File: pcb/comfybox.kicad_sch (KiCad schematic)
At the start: 20 parts, among them K1 SW_CHOC, K2 SW_CHOC, K3 SW_CHOC, K4 SW_CHOC, P1 SW_CHOC, P2 SW_CHOC, P3 SW_CHOC, P4 SW_CHOC

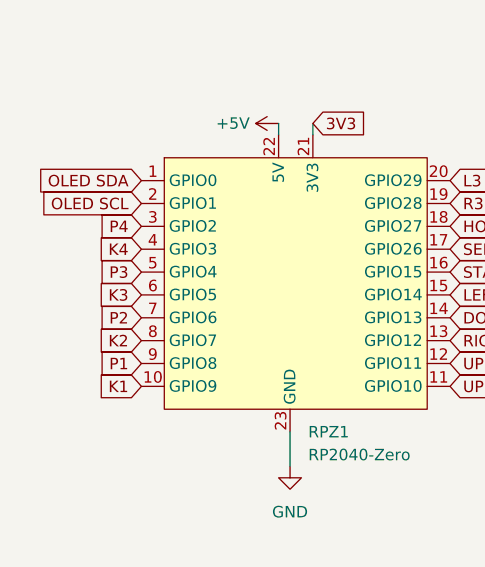
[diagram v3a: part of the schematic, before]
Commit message: improve spacing and redo tracing
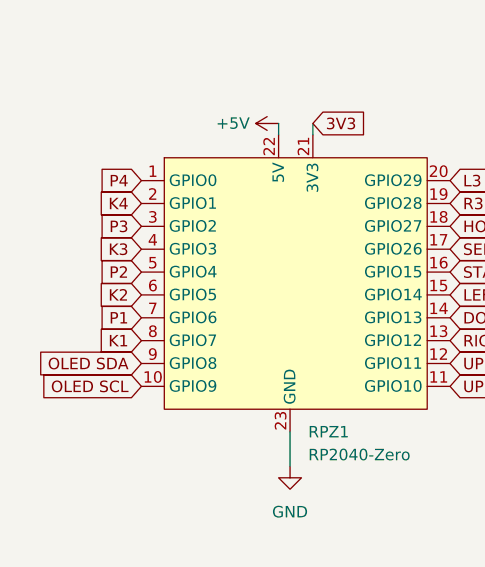
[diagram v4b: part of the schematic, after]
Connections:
- net K1: now also RPZ1.8 (GPIO7); no longer RPZ1.10 (GPIO9)
- net K2: now also RPZ1.6 (GPIO5); no longer RPZ1.8 (GPIO7)
- net K3: now also RPZ1.4 (GPIO3); no longer RPZ1.6 (GPIO5)
- net K4: now also RPZ1.2 (GPIO1); no longer RPZ1.4 (GPIO3)
- net OLED SCL: now also RPZ1.10 (GPIO9); no longer RPZ1.2 (GPIO1)
- net OLED SDA: now also RPZ1.9 (GPIO8); no longer RPZ1.1 (GPIO0)
- net P1: now also RPZ1.7 (GPIO6); no longer RPZ1.9 (GPIO8)
- net P2: now also RPZ1.5 (GPIO4); no longer RPZ1.7 (GPIO6)
- net P3: now also RPZ1.3 (GPIO2); no longer RPZ1.5 (GPIO4)
- net P4: now also RPZ1.1 (GPIO0); no longer RPZ1.3 (GPIO2)
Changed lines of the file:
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@@
     )
   )
-  (global_label "K4" (shape input) (at 45.72 64.77 180) (fields_autoplaced)
+  (global_label "K4" (shape input) (at 45.72 59.69 180) (fields_autoplaced)
     (effects (font (size 1.27 1.27)) (justify right))
-    (property "Intersheet References" "${INTERSHEET_REFS}" (id 0) (at 40.8274 64.6906 0)
+    (property "Intersheet References" "${INTERSHEET_REFS}" (id 0) (at 40.8274 59.6106 0)
       (effects (font (size 1.27 1.27)) (justify right) hide)
     )
@@
     )
   )
-  (global_label "OLED SDA" (shape input) (at 45.72 57.15 180) (fields_autoplaced)
+  (global_label "OLED SDA" (shape input) (at 45.72 77.47 180) (fields_autoplaced)
     (effects (font (size 1.27 1.27)) (justify right))
-    (property "Intersheet References" "${INTERSHEET_REFS}" (id 0) (at 33.9936 57.0706 0)
+    (property "Intersheet References" "${INTERSHEET_REFS}" (id 0) (at 33.9936 77.3906 0)
       (effects (font (size 1.27 1.27)) (justify right) hide)
     )
@@
     )
   )
-  (global_label "P4" (shape input) (at 45.72 62.23 180) (fields_autoplaced)
+  (global_label "P4" (shape input) (at 45.72 57.15 180) (fields_autoplaced)
     (effects (font (size 1.27 1.27)) (justify right))
-    (property "Intersheet References" "${INTERSHEET_REFS}" (id 0) (at 40.8274 62.1506 0)
+    (property "Intersheet References" "${INTERSHEET_REFS}" (id 0) (at 40.8274 57.0706 0)
       (effects (font (size 1.27 1.27)) (justify right) hide)
     )
@@
     )
   )
-  (global_label "P1" (shape input) (at 45.72 77.47 180) (fields_autoplaced)
+  (global_label "P1" (shape input) (at 45.72 72.39 180) (fields_autoplaced)
     (effects (font (size 1.27 1.27)) (justify right))
-    (property "Intersheet References" "${INTERSHEET_REFS}" (id 0) (at 40.8274 77.3906 0)
+    (property "Intersheet References" "${INTERSHEET_REFS}" (id 0) (at 40.8274 72.3106 0)
       (effects (font (size 1.27 1.27)) (justify right) hide)
     )
@@
     )
   )
-  (global_label "K3" (shape input) (at 45.72 69.85 180) (fields_autoplaced)
+  (global_label "K3" (shape input) (at 45.72 64.77 180) (fields_autoplaced)
     (effects (font (size 1.27 1.27)) (justify right))
-    (property "Intersheet References" "${INTERSHEET_REFS}" (id 0) (at 40.8274 69.7706 0)
+    (property "Intersheet References" "${INTERSHEET_REFS}" (id 0) (at 40.8274 64.6906 0)
       (effects (font (size 1.27 1.27)) (justify right) hide)
     )
   )
-  (global_label "P2" (shape input) (at 45.72 72.39 180) (fields_autoplaced)
+  (global_label "P2" (shape input) (at 45.72 67.31 180) (fields_autoplaced)
     (effects (font (size 1.27 1.27)) (justify right))
-    (property "Intersheet References" "${INTERSHEET_REFS}" (id 0) (at 40.8274 72.3106 0)
+    (property "Intersheet References" "${INTERSHEET_REFS}" (id 0) (at 40.8274 67.2306 0)
       (effects (font (size 1.27 1.27)) (justify right) hide)
     )
@@
     )
   )
-  (global_label "K1" (shape input) (at 45.72 80.01 180) (fields_autoplaced)
+  (global_label "K1" (shape input) (at 45.72 74.93 180) (fields_autoplaced)
     (effects (font (size 1.27 1.27)) (justify right))
-    (property "Intersheet References" "${INTERSHEET_REFS}" (id 0) (at 40.8274 79.9306 0)
+    (property "Intersheet References" "${INTERSHEET_REFS}" (id 0) (at 40.8274 74.8506 0)
       (effects (font (size 1.27 1.27)) (justify right) hide)
     )
   )
-  (global_label "P3" (shape input) (at 45.72 67.31 180) (fields_autoplaced)
+  (global_label "P3" (shape input) (at 45.72 62.23 180) (fields_autoplaced)
     (effects (font (size 1.27 1.27)) (justify right))
-    (property "Intersheet References" "${INTERSHEET_REFS}" (id 0) (at 40.8274 67.2306 0)
+    (property "Intersheet References" "${INTERSHEET_REFS}" (id 0) (at 40.8274 62.1506 0)
       (effects (font (size 1.27 1.27)) (justify right) hide)
     )
@@
     )
   )
-  (global_label "K2" (shape input) (at 45.72 74.93 180) (fields_autoplaced)
+  (global_label "K2" (shape input) (at 45.72 69.85 180) (fields_autoplaced)
     (effects (font (size 1.27 1.27)) (justify right))
-    (property "Intersheet References" "${INTERSHEET_REFS}" (id 0) (at 40.8274 74.8506 0)
+    (property "Intersheet References" "${INTERSHEET_REFS}" (id 0) (at 40.8274 69.7706 0)
       (effects (font (size 1.27 1.27)) (justify right) hide)
     )
@@
     )
   )
-  (global_label "OLED SCL" (shape input) (at 45.72 59.69 180) (fields_autoplaced)
+  (global_label "OLED SCL" (shape input) (at 45.72 80.01 180) (fields_autoplaced)
     (effects (font (size 1.27 1.27)) (justify right))
-    (property "Intersheet References" "${INTERSHEET_REFS}" (id 0) (at 34.054 59.6106 0)
+    (property "Intersheet References" "${INTERSHEET_REFS}" (id 0) (at 34.054 79.9306 0)
       (effects (font (size 1.27 1.27)) (justify right) hide)
     )

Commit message: update libs and add KS33 support
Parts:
- DOWN1, K1, K2, K3, K4, LEFT1, P1, P2, P3, P4, RIGHT1, UP1, UP2: footprint Kailh:Kailh_socket_PG1350_optional -> Switch:Kailh_PG1350_Gateron_KS27_KS33
- OLED1: footprint SSD1306:128x64OLED -> OLED:SSD1306-128x64_OLED
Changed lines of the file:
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@@
     (property "Reference" "LEFT1" (id 0) (at 120.65 64.77 0))
     (property "Value" "SW_CHOC" (id 1) (at 120.65 67.31 0))
-    (property "Footprint" "Kailh:Kailh_socket_PG1350_optional" (id 2) (at 120.65 67.31 0)
+    (property "Footprint" "Switch:Kailh_PG1350_Gateron_KS27_KS33" (id 2) (at 120.65 67.31 0)
       (effects (font (size 1.27 1.27)) hide)
     )
@@
     (property "Reference" "K4" (id 0) (at 181.61 111.76 0))
     (property "Value" "SW_CHOC" (id 1) (at 181.61 114.3 0))
-    (property "Footprint" "Kailh:Kailh_socket_PG1350_optional" (id 2) (at 181.61 114.3 0)
+    (property "Footprint" "Switch:Kailh_PG1350_Gateron_KS27_KS33" (id 2) (at 181.61 114.3 0)
       (effects (font (size 1.27 1.27)) hide)
     )
@@
     (property "Reference" "K2" (id 0) (at 140.97 111.76 0))
     (property "Value" "SW_CHOC" (id 1) (at 140.97 114.3 0))
-    (property "Footprint" "Kailh:Kailh_socket_PG1350_optional" (id 2) (at 140.97 114.3 0)
+    (property "Footprint" "Switch:Kailh_PG1350_Gateron_KS27_KS33" (id 2) (at 140.97 114.3 0)
       (effects (font (size 1.27 1.27)) hide)
     )
@@
     (property "Reference" "UP2" (id 0) (at 201.93 64.77 0))
     (property "Value" "SW_CHOC" (id 1) (at 201.93 67.31 0))
-    (property "Footprint" "Kailh:Kailh_socket_PG1350_optional" (id 2) (at 201.93 67.31 0)
+    (property "Footprint" "Switch:Kailh_PG1350_Gateron_KS27_KS33" (id 2) (at 201.93 67.31 0)
       (effects (font (size 1.27 1.27)) hide)
     )
@@
     (property "Reference" "P1" (id 0) (at 120.65 90.17 0))
     (property "Value" "SW_CHOC" (id 1) (at 120.65 92.71 0))
-    (property "Footprint" "Kailh:Kailh_socket_PG1350_optional" (id 2) (at 120.65 92.71 0)
+    (property "Footprint" "Switch:Kailh_PG1350_Gateron_KS27_KS33" (id 2) (at 120.65 92.71 0)
       (effects (font (size 1.27 1.27)) hide)
     )
@@
     (property "Reference" "K3" (id 0) (at 161.29 111.76 0))
     (property "Value" "SW_CHOC" (id 1) (at 161.29 114.3 0))
-    (property "Footprint" "Kailh:Kailh_socket_PG1350_optional" (id 2) (at 161.29 114.3 0)
+    (property "Footprint" "Switch:Kailh_PG1350_Gateron_KS27_KS33" (id 2) (at 161.29 114.3 0)
       (effects (font (size 1.27 1.27)) hide)
     )
@@
     (property "Reference" "P4" (id 0) (at 181.61 90.17 0))
     (property "Value" "SW_CHOC" (id 1) (at 181.61 92.71 0))
-    (property "Footprint" "Kailh:Kailh_socket_PG1350_optional" (id 2) (at 181.61 92.71 0)
+    (property "Footprint" "Switch:Kailh_PG1350_Gateron_KS27_KS33" (id 2) (at 181.61 92.71 0)
       (effects (font (size 1.27 1.27)) hide)
     )
@@
     (property "Reference" "P3" (id 0) (at 161.29 90.17 0))
     (property "Value" "SW_CHOC" (id 1) (at 161.29 92.71 0))
-    (property "Footprint" "Kailh:Kailh_socket_PG1350_optional" (id 2) (at 161.29 92.71 0)
+    (property "Footprint" "Switch:Kailh_PG1350_Gateron_KS27_KS33" (id 2) (at 161.29 92.71 0)
       (effects (font (size 1.27 1.27)) hide)
     )
@@
     (property "Reference" "DOWN1" (id 0) (at 140.97 64.77 0))
     (property "Value" "SW_CHOC" (id 1) (at 140.97 67.31 0))
-    (property "Footprint" "Kailh:Kailh_socket_PG1350_optional" (id 2) (at 140.97 67.31 0)
+    (property "Footprint" "Switch:Kailh_PG1350_Gateron_KS27_KS33" (id 2) (at 140.97 67.31 0)
       (effects (font (size 1.27 1.27)) hide)
     )
@@
       (effects (font (size 1.27 1.27)) (justify right))
     )
-    (property "Footprint" "SSD1306:128x64OLED" (id 2) (at 57.15 127 0)
+    (property "Footprint" "OLED:SSD1306-128x64_OLED" (id 2) (at 57.15 127 0)
       (effects (font (size 1.27 1.27)) hide)
     )
@@
     (property "Reference" "K1" (id 0) (at 120.65 111.76 0))
     (property "Value" "SW_CHOC" (id 1) (at 120.65 114.3 0))
-    (property "Footprint" "Kailh:Kailh_socket_PG1350_optional" (id 2) (at 120.65 114.3 0)
+    (property "Footprint" "Switch:Kailh_PG1350_Gateron_KS27_KS33" (id 2) (at 120.65 114.3 0)
       (effects (font (size 1.27 1.27)) hide)
     )
@@
     (property "Reference" "P2" (id 0) (at 140.97 90.17 0))
     (property "Value" "SW_CHOC" (id 1) (at 140.97 92.71 0))
-    (property "Footprint" "Kailh:Kailh_socket_PG1350_optional" (id 2) (at 140.97 92.71 0)
+    (property "Footprint" "Switch:Kailh_PG1350_Gateron_KS27_KS33" (id 2) (at 140.97 92.71 0)
       (effects (font (size 1.27 1.27)) hide)
     )
@@
     (property "Reference" "UP1" (id 0) (at 181.61 64.77 0))
     (property "Value" "SW_CHOC" (id 1) (at 181.61 67.31 0))
-    (property "Footprint" "Kailh:Kailh_socket_PG1350_optional" (id 2) (at 181.61 67.31 0)
+    (property "Footprint" "Switch:Kailh_PG1350_Gateron_KS27_KS33" (id 2) (at 181.61 67.31 0)
       (effects (font (size 1.27 1.27)) hide)
     )
@@
     (property "Reference" "RIGHT1" (id 0) (at 161.29 64.77 0))
     (property "Value" "SW_CHOC" (id 1) (at 161.29 67.31 0))
-    (property "Footprint" "Kailh:Kailh_socket_PG1350_optional" (id 2) (at 161.29 67.31 0)
+    (property "Footprint" "Switch:Kailh_PG1350_Gateron_KS27_KS33" (id 2) (at 161.29 67.31 0)
       (effects (font (size 1.27 1.27)) hide)
     )
@@
     )
     (path "/7d452c23-f08c-4cf7-8335-8028ad6af654"
-      (reference "DOWN1") (unit 1) (value "SW_CHOC") (footprint "Kailh:Kailh_socket_PG1350_optional")
+      (reference "DOWN1") (unit 1) (value "SW_CHOC") (footprint "Switch:Kailh_PG1350_Gateron_KS27_KS33")
     )
     (path "/988573a5-ea42-45d3-9cd1-0c53b1863f2e"
-      (reference "K1") (unit 1) (value "SW_CHOC") (footprint "Kailh:Kailh_socket_PG1350_optional")
+      (reference "K1") (unit 1) (value "SW_CHOC") (footprint "Switch:Kailh_PG1350_Gateron_KS27_KS33")
     )
     (path "/15ec41f1-698a-4727-beef-17758bb95787"
-      (reference "K2") (unit 1) (value "SW_CHOC") (footprint "Kailh:Kailh_socket_PG1350_optional")
+      (reference "K2") (unit 1) (value "SW_CHOC") (footprint "Switch:Kailh_PG1350_Gateron_KS27_KS33")
     )
     (path "/727e679b-e0d3-41f0-96a9-aff13fe9cbb4"
-      (reference "K3") (unit 1) (value "SW_CHOC") (footprint "Kailh:Kailh_socket_PG1350_optional")
+      (reference "K3") (unit 1) (value "SW_CHOC") (footprint "Switch:Kailh_PG1350_Gateron_KS27_KS33")
     )
     (path "/0c9cf060-b141-4ba5-9990-940b1fe0ad3f"
-      (reference "K4") (unit 1) (value "SW_CHOC") (footprint "Kailh:Kailh_socket_PG1350_optional")
+      (reference "K4") (unit 1) (value "SW_CHOC") (footprint "Switch:Kailh_PG1350_Gateron_KS27_KS33")
     )
     (path "/07666484-4233-43b6-8b39-89daeb01304c"
-      (reference "LEFT1") (unit 1) (value "SW_CHOC") (footprint "Kailh:Kailh_socket_PG1350_optional")
+      (reference "LEFT1") (unit 1) (value "SW_CHOC") (footprint "Switch:Kailh_PG1350_Gateron_KS27_KS33")
     )
     (path "/85c97a58-edb1-46c2-952a-8c8e5519c14c"
-      (reference "OLED1") (unit 1) (value "SSD1306") (footprint "SSD1306:128x64OLED")
+      (reference "OLED1") (unit 1) (value "SSD1306") (footprint "OLED:SSD1306-128x64_OLED")
     )
     (path "/67799ff0-1f81-4b52-92af-6bd82ed8650e"
@@
     )
     (path "/6da0731c-10c2-4953-ae34-8d25ba0f01a3"
-      (reference "P1") (unit 1) (value "SW_CHOC") (footprint "Kailh:Kailh_socket_PG1350_optional")
+      (reference "P1") (unit 1) (value "SW_CHOC") (footprint "Switch:Kailh_PG1350_Gateron_KS27_KS33")
     )
     (path "/cd5f6696-504a-44a7-903f-e0a955615676"
-      (reference "P2") (unit 1) (value "SW_CHOC") (footprint "Kailh:Kailh_socket_PG1350_optional")
+      (reference "P2") (unit 1) (value "SW_CHOC") (footprint "Switch:Kailh_PG1350_Gateron_KS27_KS33")
     )
     (path "/7c7f925c-6407-4bcd-88a8-6de65100b0dc"
-      (reference "P3") (unit 1) (value "SW_CHOC") (footprint "Kailh:Kailh_socket_PG1350_optional")
+      (reference "P3") (unit 1) (value "SW_CHOC") (footprint "Switch:Kailh_PG1350_Gateron_KS27_KS33")
     )
     (path "/7936b223-b7bd-4515-a0fe-d144ab49b05f"
-      (reference "P4") (unit 1) (value "SW_CHOC") (footprint "Kailh:Kailh_socket_PG1350_optional")
+      (reference "P4") (unit 1) (value "SW_CHOC") (footprint "Switch:Kailh_PG1350_Gateron_KS27_KS33")
     )
     (path "/e76e705b-1acd-49f8-917b-6c87709d07ea"
-      (reference "RIGHT1") (unit 1) (value "SW_CHOC") (footprint "Kailh:Kailh_socket_PG1350_optional")
+      (reference "RIGHT1") (unit 1) (value "SW_CHOC") (footprint "Switch:Kailh_PG1350_Gateron_KS27_KS33")
     )
     (path "/1c88fcf1-197e-4669-a023-1e1afa0350b1"
@@
     )
     (path "/ce8a3f3c-1400-4998-82a3-592704bb4069"
-      (reference "UP1") (unit 1) (value "SW_CHOC") (footprint "Kailh:Kailh_socket_PG1350_optional")
+      (reference "UP1") (unit 1) (value "SW_CHOC") (footprint "Switch:Kailh_PG1350_Gateron_KS27_KS33")
     )
     (path "/2bf912dd-be99-4601-b086-b60d1966be39"
-      (reference "UP2") (unit 1) (value "SW_CHOC") (footprint "Kailh:Kailh_socket_PG1350_optional")
-    )
-  )
+      (reference "UP2") (unit 1) (value "SW_CHOC") (footprint "Switch:Kailh_PG1350_Gateron_KS27_KS33")
+    )
+  )
